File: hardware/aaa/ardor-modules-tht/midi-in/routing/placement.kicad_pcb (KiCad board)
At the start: 2 copper layers, 85 x 70 mm, 20 parts, among them J101 POWER INPUT + UART OUTPUT TO 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, J202 MIDI INPUT FROM DIN SOCKET, J203 METAL CASE BOND + GROUND, U201 onsemi H11L1M

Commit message: fix(hardware): use Hestore TVS diodes in hand-assembly modules
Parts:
- D202: value SA5.0CA-E3/54 -> 1.5KE6.8CA; footprint Diode_THT:D_DO-15_P10.16mm_Horizontal -> Ardor_THT:D_TVS_DC_1.5KE_P15.24mm
- moved D202 2.54 mm to (56.0, 72.6)

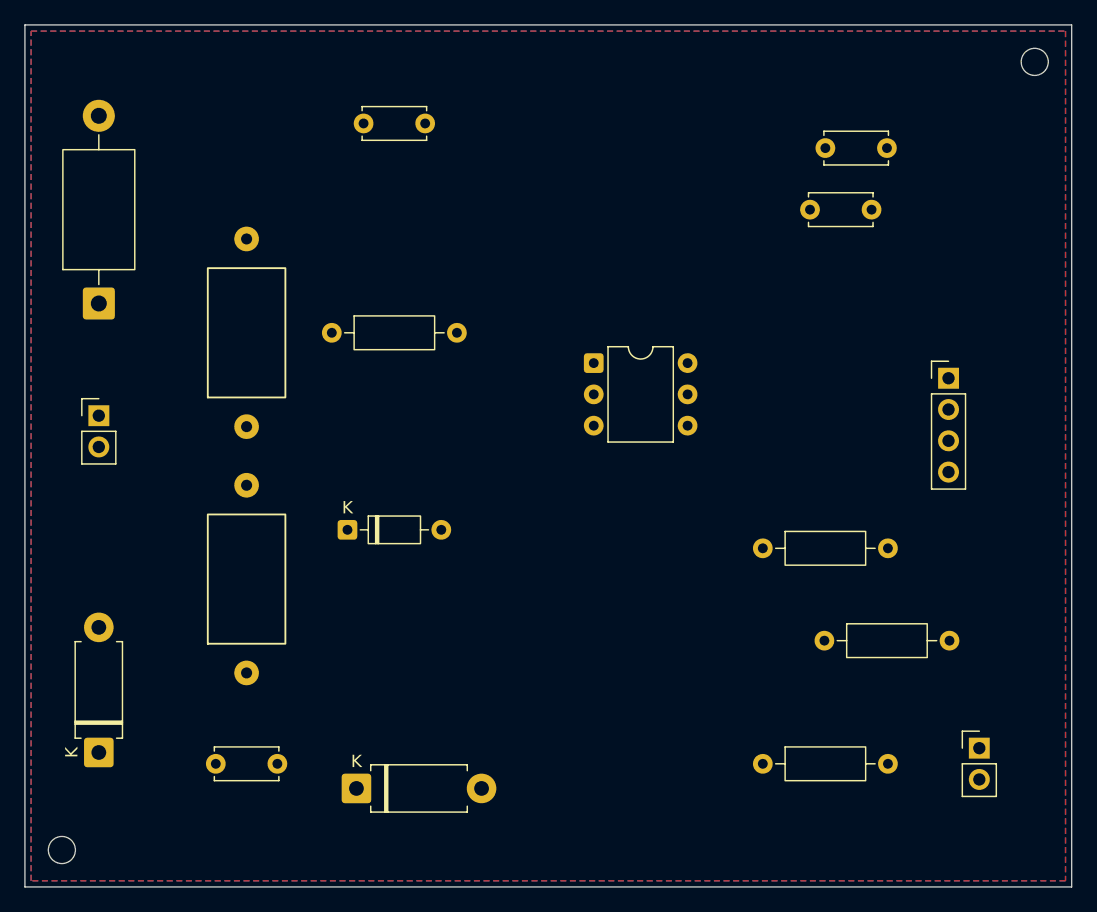
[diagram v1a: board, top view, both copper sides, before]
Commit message: feat(hardware): compact layouts and adopt Hestore module packages
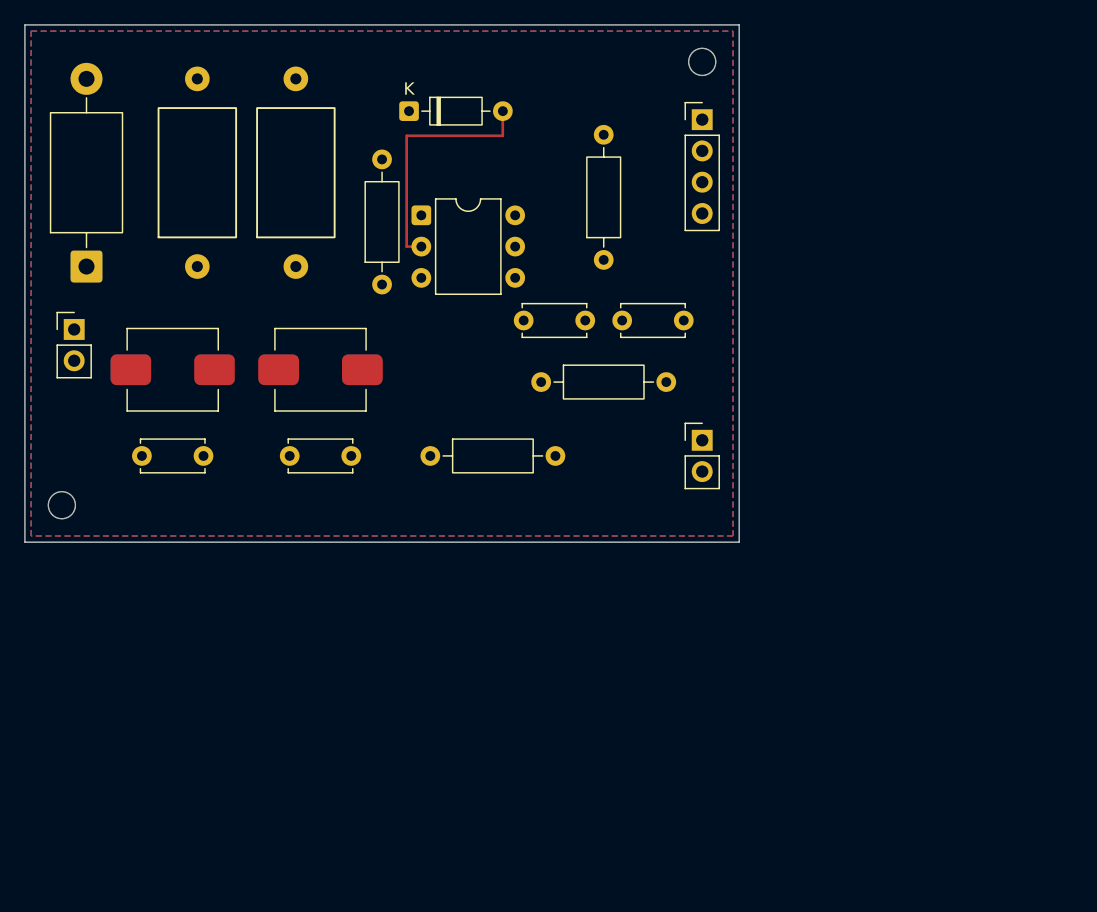
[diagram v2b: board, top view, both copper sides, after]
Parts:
- D203, D204: value SA24CA-E3/54 -> SMDJ24CA; footprint Diode_THT:D_DO-15_P10.16mm_Horizontal -> Ardor_THT:D_SMC_Bidirectional_Handsolder
- moved R101 36.8 mm to (82.9, 85.0)
- moved D201 34.4 mm to (81.2, 57.0)
- moved D204 34.1 mm to (74.0, 78.0)
- moved J203 33.6 mm to (105.0, 83.7)
- moved FB202 33.2 mm to (72.0, 69.6)
- moved C202 32.4 mm to (59.5, 85.0)
- moved D203 31.7 mm to (62.0, 78.0), turned to 0 degrees
- moved R203 31.1 mm to (91.9, 79.0)
- moved J101 29.0 mm to (105.0, 57.7)
- moved H1 28.0 mm to (53.0, 89.0)
- moved H2 27.0 mm to (105.0, 53.0)
- moved R202 26.7 mm to (97.0, 69.1), turned to 90 degrees
- moved C203 25.7 mm to (71.5, 85.0)
- moved C201 24.9 mm to (90.5, 74.0)
- moved C204 21.6 mm to (98.5, 74.0)
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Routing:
- net Net-(D201-A): track 0.00 -> 20.0 mm
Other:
- board size 85 x 70 mm -> 58 x 42 mm
